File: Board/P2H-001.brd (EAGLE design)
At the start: 72 x 72 mm, 26 parts, among them IC1 LTC485N, IC2 74LS07N, IC3 74LS157N, IC4 LTC485N, IC5 TLC5941NT, U1 ARDUINO_PRO_MINI

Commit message: Brush up.
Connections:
- net GND: now also CN2.4
- net VCC: now also CN2.1; no longer CN2.4
- net VDD: no longer CN2.1
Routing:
- net LED3B: track 30.3 -> 206.3 mm, vias 0 -> 3
- net N$5: track 68.3 -> 198.0 mm, vias 1 -> 6
- net N$2: track 24.3 -> 148.4 mm, vias 0 -> 9
- net VDD: track 162.2 -> 70.9 mm
- net TX+: track 82.3 -> 152.5 mm
- net GND: track 284.5 -> 339.7 mm, vias 1 -> 0
- net N$8: track 42.0 -> 90.8 mm, vias 2 -> 3
- net LEDA: track 106.4 -> 153.7 mm
- net TX-: track 80.9 -> 121.8 mm, vias 4 -> 3
- net A3: track 44.8 -> 76.7 mm, vias 2 -> 4
- net N$12: track 114.8 -> 144.1 mm
- net N$7: track 37.2 -> 65.3 mm, vias 0 -> 4
- net MODE: track 127.5 -> 155.4 mm, vias 4 -> 3
- net A5: track 76.0 -> 48.3 mm, vias 2 -> 1
- net VR: track 56.2 -> 73.7 mm, vias 2 -> 1
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
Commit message: Hotfix.
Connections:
- new net N$10: IC5.17, SV2.3
- net SIN: no longer SV2.3
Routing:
- net LED3B: track 206.3 -> 30.3 mm, vias 3 -> 0
- net N$5: track 198.0 -> 53.6 mm, vias 6 -> 1
- net N$2: track 148.4 -> 30.9 mm, vias 9 -> 3
- net A2: track 31.9 -> 117.2 mm, vias 0 -> 7
- net TX-: track 121.8 -> 198.3 mm, vias 3 -> 1
- net GND: track 339.7 -> 269.9 mm
- net A3: track 76.7 -> 135.1 mm, vias 4 -> 3
- net GSCLCK: track 107.2 -> 160.5 mm, vias 0 -> 1
- net N$8: track 90.8 -> 41.6 mm, vias 3 -> 0
- net GDETECT: track 19.0 -> 64.5 mm, vias 0 -> 3
- net N$14: track 151.0 -> 108.5 mm, vias 2 -> 0
- net BLANK: track 131.9 -> 92.7 mm
- net MODE: track 155.4 -> 116.7 mm
- net TX: track 32.6 -> 70.9 mm, vias 0 -> 2
- net A5: track 48.3 -> 81.5 mm, vias 1 -> 5
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
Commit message: Board and Doc update.
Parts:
- added JP2: (no value), pinhead:1X02
- moved R2 40.7 mm to (12.7, 38.1), turned to 90 degrees
- moved C2 20.3 mm to (53.3, 35.6)
- moved R1 17.8 mm to (53.3, 53.3)
- moved C4 15.3 mm to (24.1, 49.5)
- moved R6 7.62 mm to (53.3, 58.4)
- moved C6 7.62 mm to (41.9, 7.62)
- moved C1 2.54 mm to (53.3, 63.5)
- moved IC1 2.54 mm to (16.5, 49.5)
- moved R5 2.54 mm to (53.3, 48.3)
- moved C3 1.27 mm to (29.2, 49.5)
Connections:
- net MIDIRX: now also JP2.2
- net N$1: now also JP2.1
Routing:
- net A2: track 117.2 -> 30.4 mm, vias 7 -> 1
- net A3: track 135.1 -> 51.8 mm, vias 3 -> 0
- net GND: track 269.9 -> 353.0 mm
- net BLANK: track 92.7 -> 175.3 mm
- net VDD: track 75.4 -> 120.7 mm, vias 2 -> 4
- net A5: track 81.5 -> 37.8 mm, vias 5 -> 2
- net SIN: track 57.3 -> 99.6 mm, vias 0 -> 5
- net GDETECT: track 64.5 -> 22.5 mm, vias 3 -> 0
- net TX-: track 198.3 -> 158.4 mm, vias 1 -> 4
- net LEDA: track 140.1 -> 102.9 mm, vias 1 -> 3
- net GSCLCK: track 160.5 -> 132.2 mm, vias 1 -> 2
- net TX: track 70.9 -> 43.5 mm, vias 2 -> 1
- net RX-: track 78.6 -> 105.0 mm, vias 2 -> 0
- net XLAT: track 171.7 -> 149.6 mm, vias 1 -> 0
- net GPIO: track 68.8 -> 46.8 mm
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
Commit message: Jumper to Switch.
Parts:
- removed JP1, JP2: (no value), pinhead:1X02
- added S1: TL39PO, switch:TL3XPO
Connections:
- net MIDIRX: now also S1.1; no longer JP2.2
- net N$1: now also S1.3; no longer JP1.2, JP2.1
- net RX: now also S1.2; no longer JP1.1
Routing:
- net TX-: track 158.4 -> 109.9 mm
- net MODE: track 103.3 -> 150.3 mm, vias 5 -> 2
- net VCC: track 307.0 -> 262.3 mm
- net BLANK: track 175.3 -> 131.3 mm, vias 2 -> 3
- net GND: track 353.0 -> 311.5 mm
- net VDD: track 120.7 -> 82.4 mm, vias 4 -> 3
- net GSCLCK: track 132.2 -> 94.1 mm, vias 2 -> 1
- net RX-: track 105.0 -> 73.7 mm
- net LEDA: track 102.9 -> 125.5 mm, vias 3 -> 1
- net SIN: track 99.6 -> 78.0 mm, vias 5 -> 4
- net VR: track 78.5 -> 57.3 mm, vias 1 -> 2
- net N$5: track 53.6 -> 74.4 mm, vias 3 -> 0
- net N$14: track 128.0 -> 111.4 mm
- net XLAT: track 149.6 -> 136.3 mm, vias 0 -> 1
- net SWMIN: track 40.3 -> 27.7 mm, vias 1 -> 0
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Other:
- board text added: "P2H 1.0.0"
- board text removed: "PINEAPPLE.CC P2H 1.0.0/2015"

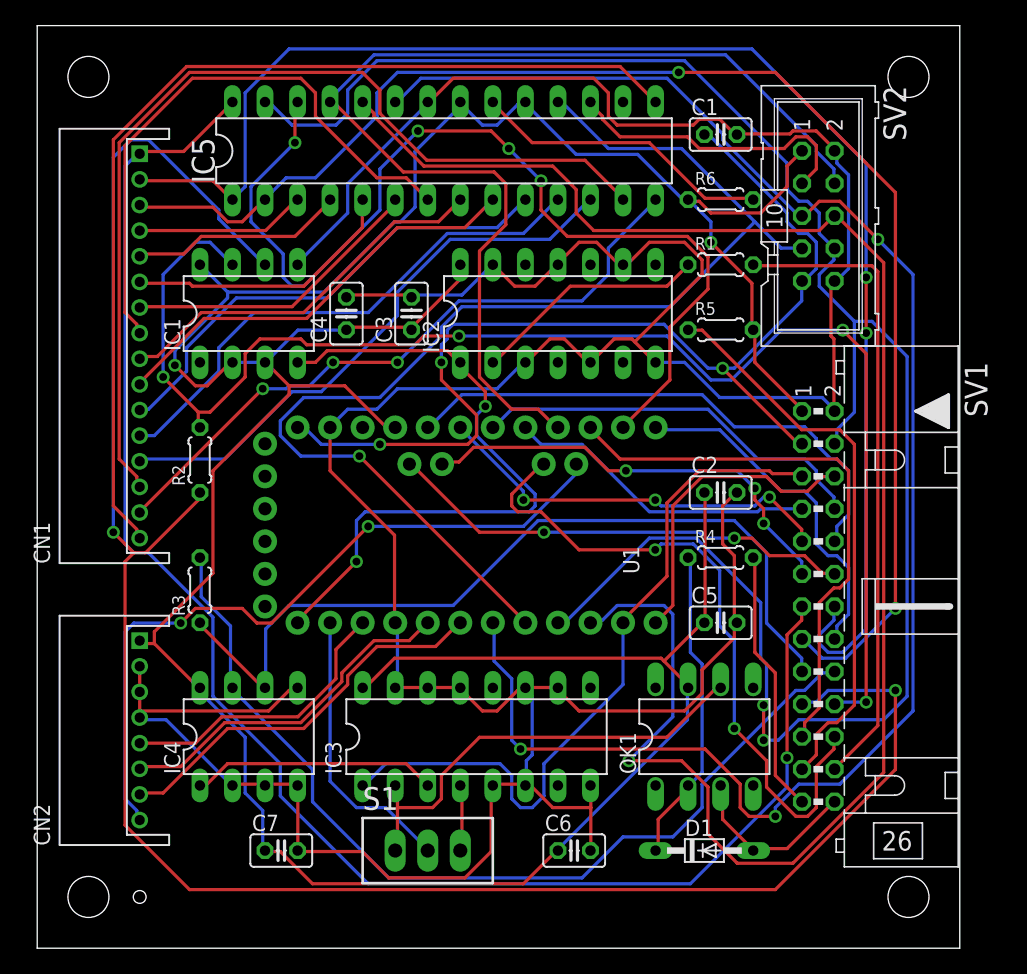
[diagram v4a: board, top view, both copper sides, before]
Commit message: changed circuit of mdetect.
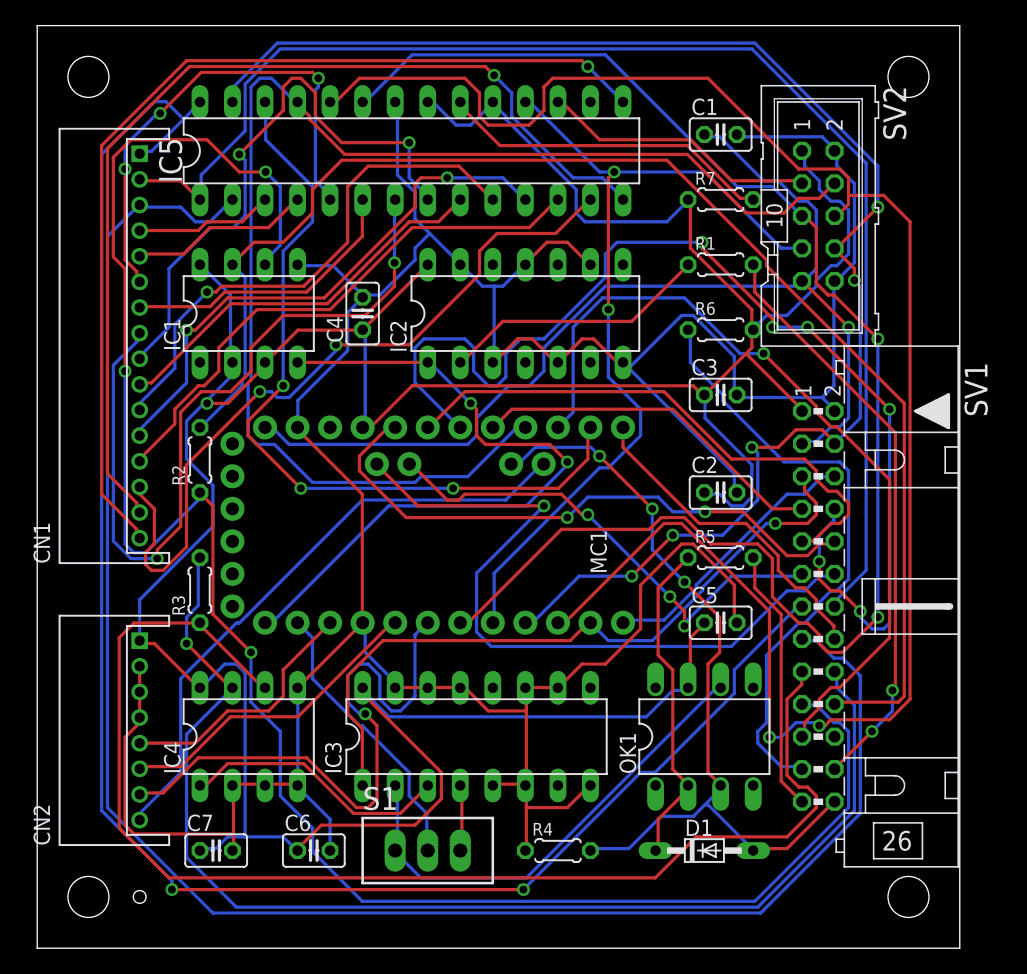
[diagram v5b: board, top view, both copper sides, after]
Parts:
- removed U1: ARDUINO_PRO_MINI, SparkFun-Boards:ARDUINO_PRO_MINI
- added MC1: ARDUINO_PRO_MINI, SparkFun-Boards:ARDUINO_PRO_MINI
- added R7: 4.7k, resistor:0204/5
- C1: value 0.1u -> 104
- C2, C3, C4, C5, C6, C7: value 0.01u -> 103
- R4: value 220 -> 22k
- R6: value 4.7k -> 220
- moved R4 26.2 mm to (40.6, 7.62)
- moved C3 25.0 mm to (53.3, 43.2), turned to 0 degrees
- moved C6 20.3 mm to (21.6, 7.62)
- moved R5 17.8 mm to (53.3, 30.5)
- moved R6 10.2 mm to (53.3, 48.3)
- moved C7 5.08 mm to (14.0, 7.62)
- moved IC2 2.54 mm to (38.1, 49.5)
- moved IC5 2.54 mm to (29.2, 62.2)
- moved C4 1.27 mm to (25.4, 49.5)
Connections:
- removed net MDETECT: SV1.22, U1.A7
- net A0: now also MC1.17; no longer U1.17
- net A1: now also MC1.18; no longer U1.18
- net A2: now also MC1.19; no longer U1.19
- net A3: now also MC1.20; no longer U1.20
- net A4: now also MC1.A4; no longer U1.A4
- net A5: now also MC1.A5; no longer U1.A5
- net BLANK: now also MC1.7; no longer U1.7
- net GDETECT: now also MC1.12; no longer U1.12
- net GND: now also MC1.23, MC1.4, R4.1; no longer U1.23, U1.4
- net GPIO: now also MC1.15; no longer U1.15
- net GSCLCK: now also MC1.8; no longer U1.8
- net MIDIRXA: now also R5.2; no longer R4.2
- net MIDIRXK: now also MC1.A7, R4.2
- net MODE: now also MC1.9; no longer U1.9
- net N$13: now also R5.1; no longer R4.1
- net N$37: now also R7.2; no longer R6.2
- net N$4: now also R6.1; no longer R5.1
- net RX: now also MC1.2; no longer U1.2
- net SCLCK: now also MC1.16; no longer U1.16
- net SIN: now also MC1.14; no longer U1.14
- net SWMAX: now also MC1.6; no longer U1.6
- net SWMIN: now also MC1.5; no longer U1.5
- net SWRST: now also MC1.3; no longer U1.3
- net TX: now also MC1.1; no longer U1.1
- net VCC: now also MC1.21, R6.2, R7.1; no longer R5.2, R6.1, U1.21
- net VDD: now also MC1.24; no longer U1.24
- net VR: now also MC1.A6; no longer U1.A6
- net XBAR: now also MC1.11; no longer U1.11
- net XDETECT: now also MC1.13; no longer U1.13
- net XLAT: now also MC1.10; no longer U1.10
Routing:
- net A1: track 31.4 -> 90.7 mm, vias 0 -> 6
- net MDETECT: track 52.7 -> 0.00 mm, vias 2 -> 0
- net MIDIRXK: track 14.1 -> 64.0 mm, vias 0 -> 3
- net GND: track 311.5 -> 275.2 mm
- net MODE: track 150.3 -> 115.7 mm, vias 2 -> 5
- net RX+: track 66.1 -> 99.7 mm
- net N$14: track 111.4 -> 138.5 mm, vias 2 -> 0
- net N$24: track 51.7 -> 77.8 mm, vias 3 -> 1
- net GSCLCK: track 94.1 -> 68.0 mm, vias 1 -> 2
- net RX-: track 73.7 -> 95.2 mm, vias 0 -> 1
- net A5: track 36.7 -> 57.2 mm, vias 2 -> 1
- net GPIO: track 44.2 -> 63.4 mm, vias 0 -> 1
- net SCLCK: track 86.2 -> 103.6 mm
- net LED2B: track 21.7 -> 38.8 mm, vias 0 -> 3
- net SIN: track 78.0 -> 61.4 mm, vias 4 -> 3
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
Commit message: changed detector cicuits for midi in and out.
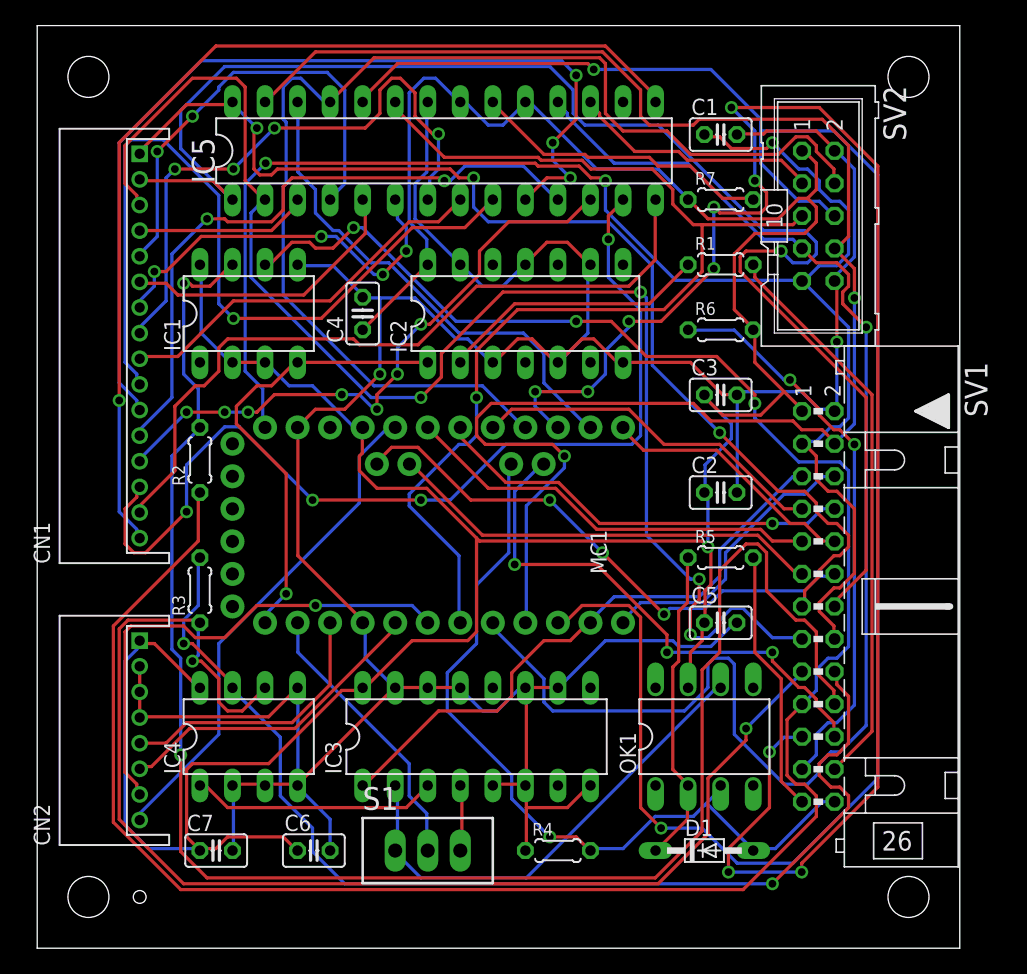
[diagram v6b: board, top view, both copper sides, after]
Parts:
- moved IC5 2.54 mm to (31.8, 62.2)
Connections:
- removed net A3: MC1.20, SV1.10
- removed net XDETECT: MC1.13, SV1.16
- new net MDETECT: MC1.A6, SV1.22
- new net MISO: MC1.15, SV1.21
- net GPIO: now also MC1.13, SV1.10; no longer MC1.15, SV1.21
- net VDD: now also SV1.16
- net VR: now also MC1.20; no longer MC1.A6
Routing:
- net MISO: track 0.00 -> 131.4 mm, vias 0 -> 10
- net A1: track 90.7 -> 33.2 mm, vias 6 -> 1
- net LEDA: track 134.3 -> 87.4 mm, vias 2 -> 3
- net A3: track 46.6 -> 0.00 mm, vias 2 -> 0
- net VDD: track 83.7 -> 127.4 mm, vias 1 -> 3
- net GPIO: track 63.4 -> 20.3 mm, vias 1 -> 0
- net GSCLCK: track 68.0 -> 110.3 mm, vias 2 -> 1
- net MDETECT: track 0.00 -> 41.4 mm, vias 0 -> 3
- net BLANK: track 118.8 -> 86.2 mm, vias 2 -> 1
- net N$7: track 41.4 -> 73.9 mm, vias 1 -> 3
- net N$6: track 31.1 -> 62.6 mm, vias 0 -> 1
- net N$14: track 138.5 -> 112.2 mm, vias 0 -> 4
- net XDETECT: track 25.9 -> 0.00 mm
- net TX-: track 108.2 -> 133.8 mm, vias 0 -> 2
- net TX+: track 149.3 -> 174.8 mm
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
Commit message: Layout change.
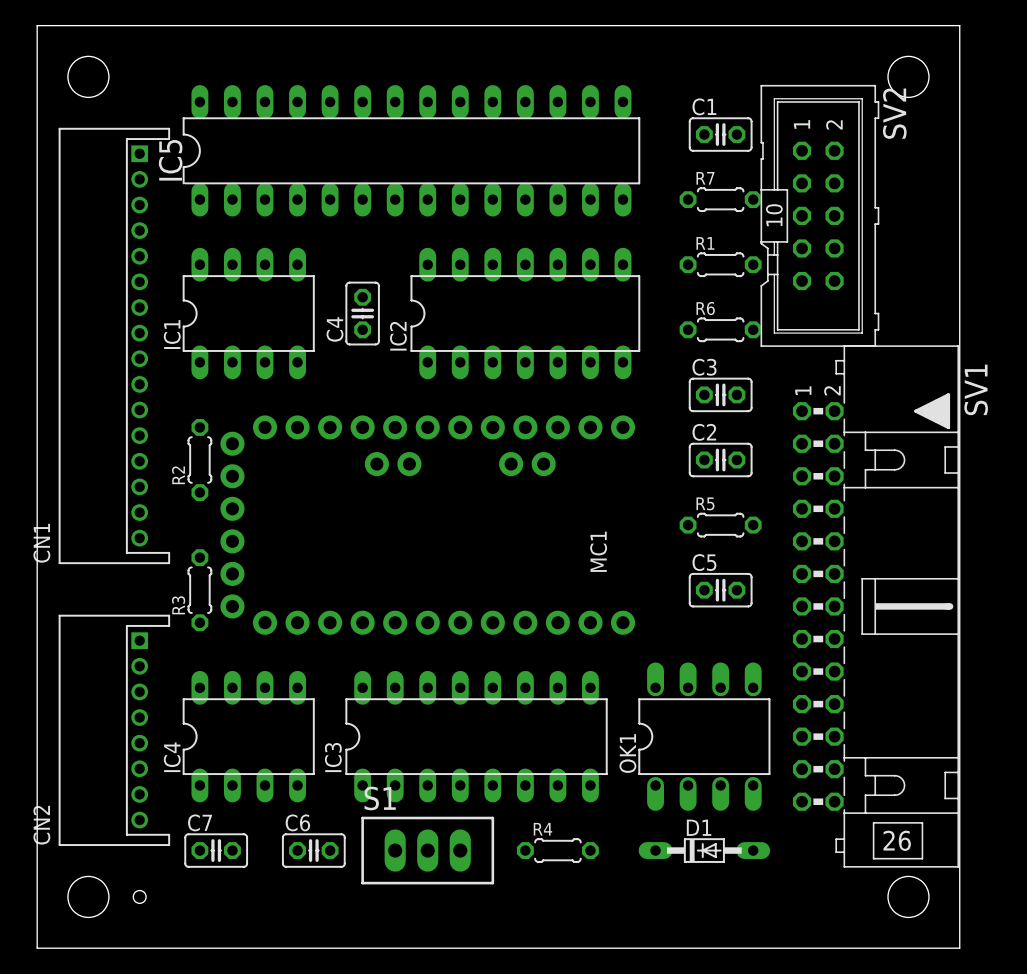
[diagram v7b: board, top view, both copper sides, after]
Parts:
- moved C5 2.54 mm to (53.3, 27.9)
- moved R5 2.54 mm to (53.3, 33.0)
- moved C2 2.54 mm to (53.3, 38.1)
- moved IC5 2.54 mm to (29.2, 62.2)
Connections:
- removed net MDETECT: MC1.A6, SV1.22
- removed net MISO: MC1.15, SV1.21
- new net N$4: MC1.A6, SV1.21
- net A0: now also SV1.11; no longer SV1.7
- net A1: now also SV1.13; no longer SV1.8
- net A2: now also SV1.15; no longer SV1.9
- net A4: now also SV1.17; no longer SV1.11
- net A5: now also SV1.19; no longer SV1.12
- net GDETECT: now also SV1.7; no longer SV1.6
- net GND: now also SV1.4, SV1.6, SV1.8
- net GPIO: now also SV1.9; no longer SV1.10
- net LEDA: now also SV1.10; no longer SV1.13
- net MIDIRXA: now also SV1.24; no longer SV1.25
- net MIDIRXK: no longer MC1.A7
- net MIDITX: now also SV1.25; no longer SV1.24
- net MODE: no longer SV1.4
- net N$12: now also SV1.12; no longer SV1.14
- net N$14: now also SV1.14; no longer SV1.15
- net RX+: now also R3.2, SV1.16; no longer R3.1, SV1.17
- net RX-: now also R3.1; no longer R3.2
- net TX+: now also SV1.20; no longer SV1.19
- net TX-: now also SV1.22; no longer SV1.20
- net VDD: now also SV1.5; no longer SV1.16
- net XBAR: no longer SV1.5
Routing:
- net GND: track 265.9 -> 0.00 mm, vias 2 -> 0
- net VCC: track 253.3 -> 0.00 mm, vias 1 -> 0
- net TX+: track 174.8 -> 0.00 mm, vias 3 -> 0
- net XLAT: track 148.3 -> 0.00 mm, vias 2 -> 0
- net TX-: track 133.8 -> 0.00 mm, vias 2 -> 0
- net MISO: track 131.4 -> 0.00 mm, vias 10 -> 0
- net MODE: track 129.8 -> 0.00 mm, vias 2 -> 0
- net VDD: track 127.4 -> 0.00 mm, vias 3 -> 0
- net N$12: track 114.5 -> 0.00 mm, vias 1 -> 0
- net N$14: track 112.2 -> 0.00 mm, vias 4 -> 0
- net GSCLCK: track 110.3 -> 0.00 mm, vias 1 -> 0
- net RX+: track 99.3 -> 0.00 mm, vias 2 -> 0
- net SCLCK: track 93.5 -> 0.00 mm
- net LEDA: track 87.4 -> 0.00 mm, vias 3 -> 0
- net RX-: track 87.2 -> 0.00 mm, vias 2 -> 0
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
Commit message: Fixed panel LED layout.
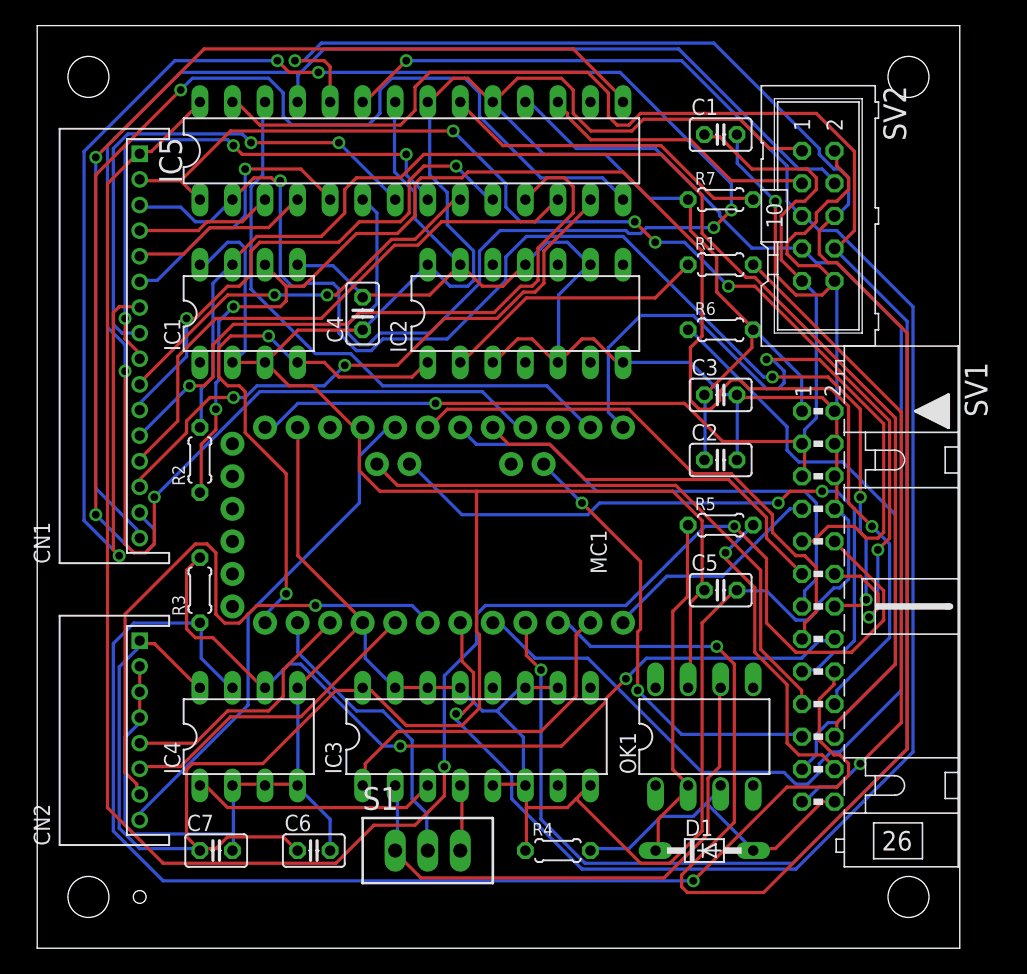
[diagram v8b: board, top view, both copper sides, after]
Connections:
- net LED2B renamed LED3
- net LED2G renamed LED2
- net LEDA renamed G10
- net N$12 renamed G11
- net N$14 renamed G12
- net N$25 renamed LEDMAIN
- net N$9 renamed LED1
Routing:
- net GND: track 0.00 -> 301.7 mm, vias 0 -> 1
- net VCC: track 0.00 -> 282.2 mm
- net LED3R: track 0.00 -> 162.2 mm, vias 0 -> 5
- net XLAT: track 0.00 -> 159.6 mm, vias 0 -> 2
- net MODE: track 0.00 -> 155.8 mm, vias 0 -> 1
- net G10: track 0.00 -> 154.5 mm, vias 0 -> 2
- net BLANK: track 0.00 -> 142.8 mm, vias 0 -> 2
- net SCLCK: track 0.00 -> 138.4 mm, vias 0 -> 2
- net TX+: track 0.00 -> 116.8 mm, vias 0 -> 3
- net TX-: track 0.00 -> 107.6 mm
- net GSCLCK: track 0.00 -> 105.7 mm
- net RX-: track 0.00 -> 100.5 mm, vias 0 -> 1
- net G12: track 0.00 -> 98.4 mm, vias 0 -> 4
- net G11: track 0.00 -> 94.9 mm, vias 0 -> 6
- net N$24: track 0.00 -> 90.0 mm, vias 0 -> 2
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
